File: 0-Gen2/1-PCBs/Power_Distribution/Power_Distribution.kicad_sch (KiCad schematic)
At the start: 33 parts, among them IC1 ACS713ELCTR-30A-T, IC2 ACS713ELCTR-30A-T, IC3 ACS713ELCTR-30A-T, IC4 ACS713ELCTR-30A-T, IC5 ACS713ELCTR-30A-T, IC6 ACS713ELCTR-30A-T, IC7 ACS713ELCTR-30A-T, IC8 ACS713ELCTR-30A-T, J1 1098169, J2 1098169, J3 Conn_01x08, J4 1986660-2, J5 Conn_01x06, J6 1098169, J7 1098169, J8 Conn_01x02, J9 Conn_01x08

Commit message: [add] MLU2 progress, [bugfix] depth sensor
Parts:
- removed J5: Conn_01x06, Connector_PinHeader_2.54mm:PinHeader_1x06_P2.54mm_Vertical, symbol Connector_Generic:Conn_01x06
- removed J8: Conn_01x02, Connector_PinHeader_2.54mm:PinHeader_1x02_P2.54mm_Vertical, symbol Connector_Generic:Conn_01x02
- added Cf10, Cf11, Cf12, Cf13, Cf14, Cf15, Cf16, Cf9: 100 µF, Capacitor_SMD:C_0805_2012Metric_Pad1.18x1.45mm_HandSolder, symbol Device:C
- added H1: IDC Cable, symbol Mechanical:MountingHole
- added J10, J11, J12, J13, J14, J15, J16, J17: 430450228, Imported_Footprints:CONN_SD-43045-010_02_MOL, symbol Imported:430450228
- added J18: SBH11-PBPC-D10-ST-BK, Imported_Footprints:SULLINS_SBH11-PBPC-D10-ST-BK, symbol Imported_Symbols:SBH11-PBPC-D10-ST-BK
- added JP1, JP2: Jumper_2_Bridged, Jumper:SolderJumper-2_P1.3mm_Bridged2Bar_RoundedPad1.0x1.5mm, symbol Jumper:Jumper_2_Bridged
- added LED1, LED10, LED11, LED12, LED2, LED3, LED4, LED5, LED6, LED7, LED8, LED9: 1655, LED_SMD:LED_LiteOn_LTST-E563C_PLCC4_5.0x5.0mm_P3.2mm_HandSoldering, symbol Imported_Symbols:1655
- added R1, R2: 10k, Resistor_SMD:R_0805_2012Metric_Pad1.20x1.40mm_HandSolder, symbol Device:R_US
- added U1, U2: MCP9808_MSOP, Package_SO:MSOP-8_3x3mm_P0.65mm, symbol Sensor_Temperature:MCP9808_MSOP
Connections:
- net COM: now also JP2.1 (A)
- net GND: now also Cf10.2, Cf11.2, Cf12.2, Cf13.2, Cf14.2, Cf15.2, Cf16.2, Cf9.2, J10.2, J11.2, J12.2, J13.2, J14.2, J15.2, J16.2, J17.2, J18.12, J18.20, JP2.2 (B), LED1.1 (VSS), LED10.1 (VSS), LED11.1 (VSS), LED12.1 (VSS), LED2.1 (VSS), LED3.1 (VSS), LED4.1 (VSS), LED5.1 (VSS), LED6.1 (VSS), LED7.1 (VSS), LED8.1 (VSS), LED9.1 (VSS), R1.2, R2.2, U1.4 (GND), U1.5 (A2), U2.4 (GND), U2.6 (A1)
- net REF: now also JP1.1 (A)
- net SCL: now also J18.2, U1.2 (SCL), U2.2 (SCL)
- net SDA: now also J18.4, U1.1 (SDA), U2.1 (SDA)
- net VIout1: now also Cf9.1
- net VIout2: now also Cf10.1
- net VIout3: now also Cf11.1
- net VIout4: now also Cf12.1
- net VIout5: now also Cf13.1
- net VIout6: now also Cf14.1
- net VIout7: now also Cf15.1
- net VIout8: now also Cf16.1
- net 5V renamed +5V
- net +5V: now also J18.14, J18.16, JP1.2 (B), LED1.3 (VDD), LED10.3 (VDD), LED11.3 (VDD), LED12.3 (VDD), LED2.3 (VDD), LED3.3 (VDD), LED4.3 (VDD), LED5.3 (VDD), LED6.3 (VDD), LED7.3 (VDD), LED8.3 (VDD), LED9.3 (VDD)
- new net: LED3.4 (DOUT), LED4.2 (DIN)
- new net: LED10.2 (DIN), LED9.4 (DOUT)
- new net: LED5.4 (DOUT), LED6.2 (DIN)
- new net: LED6.4 (DOUT), LED7.2 (DIN)
- new net: LED10.4 (DOUT), LED11.2 (DIN)
- new net: LED11.4 (DOUT), LED12.2 (DIN)
- new net: LED7.4 (DOUT), LED8.2 (DIN)
- new net: LED1.4 (DOUT), LED2.2 (DIN)
- new net +3.3V: J18.18, R1.1, R2.1, U1.6 (A1), U1.7 (A0), U1.8 (V_{DD}), U2.5 (A2), U2.7 (A0), U2.8 (V_{DD})
- new net NEO_PASS1: LED4.4 (DOUT), LED5.2 (DIN)
- new net NEO_PASS2: LED8.4 (DOUT), LED9.2 (DIN)
- new net PWM0: J10.1, J18.1
- new net PWM1: J12.1, J18.3
- new net PWM2: J14.1, J18.5
- new net PWM3: J16.1, J18.7
- new net PWM4: J11.1, J18.9
- new net PWM5: J13.1, J18.11
- new net PWM6: J15.1, J18.13
- new net PWM7: J17.1, J18.15
- new net outNEO_CTRL_MOOD: J18.8, LED12.4 (DOUT)
- new net outNEO_CTRL_SIG: J18.19, LED2.4 (DOUT)
- new net toNEO_CTRL_MOOD: J18.6, LED3.2 (DIN)
- new net toNEO_CTRL_SIG: J18.17, LED1.2 (DIN)
- no-connect marks 0 -> 5
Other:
- note added: "Analog noise filter"
- note added: "I2C @ 0x1B format: 0011(A2)(A1)(A0)"
- note added: "I2C @ 0x1D format: 0011(A2)(A1)(A0)"
- note added: "I2C @ 0x48"
- note added: "Integrated MCP9808 #1"
- note added: "Integrated MCP9808 #2"
- note added: "Interconnect to MLU"
- note added: "Leak sensor on this board? Humidity sensor on this board?"
- note added: "PWM Thruster Interface"
- note added: "Power Connectors To ESCs"
- note added: "https://learn.adafruit.com/adafruit-ads7830-8-channel-8-bit-adc/pinouts"
- note removed: "Connectors To ESCs"
- moved on the sheet: Cb1, Cb2, Cb3, Cb4, Cb5, Cb6, Cb7, Cb8, Cf1, Cf2, Cf3, Cf4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

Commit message: management2 updates
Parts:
- added JP3: Jumper_3_Bridged12, Jumper:SolderJumper-3_P1.3mm_Bridged2Bar12_RoundedPad1.0x1.5mm, symbol Jumper:Jumper_3_Bridged12
- added R3: 2.2k Array, Imported_Footprints:RES_EXB2HV_1506x8, symbol Imported_Symbols:EXB-2HV222JV
- added R4: 3.9k Array, Imported_Footprints:RES_EXB2HV_1506x8, symbol Imported_Symbols:EXB-2HV222JV
- Cf1: value 100 µF -> 100 nF; Supplier 1 https://www.digikey.com/en/products/detail/murata-electroni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 -> https://www.digikey.com/en/products/detail/yageo/CC0805KRX7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; Supplier 1 S/N 490-13980-1-ND -> 311-1140-1-ND
- Cf10, Cf11, Cf12, Cf13, Cf14, Cf15, Cf16, Cf9: value 100 µF -> 1 µF; Supplier 1 https://www.digikey.com/en/products/detail/murata-electroni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 -> https://www.digikey.com/en/products/detail/samsung-electro-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; Supplier 1 S/N 490-13980-1-ND -> 1276-1029-1-ND
- Cf2, Cf3, Cf4, Cf5, Cf6, Cf7, Cf8: value 100 µF -> 100nF; Supplier 1 https://www.digikey.com/en/products/detail/murata-electroni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 -> https://www.digikey.com/en/products/detail/yageo/CC0805KRX7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; Supplier 1 S/N 490-13980-1-ND -> 311-1140-1-ND
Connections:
- net +3.3V: now also JP1.2 (B), JP3.2 (C)
- net +5V: now also JP3.3 (B); no longer J3.1 (Pin_1), JP1.2 (B)
- net GND: now also R4.10, R4.11, R4.12, R4.13, R4.14, R4.15, R4.16, R4.9
- net VIout1: now also R3.1; no longer J9.8 (Pin_8)
- net VIout2: now also R3.2; no longer J9.7 (Pin_7)
- net VIout3: now also R3.3; no longer J9.6 (Pin_6)
- net VIout4: now also R3.4; no longer J9.5 (Pin_5)
- net VIout5: now also R3.5; no longer J9.4 (Pin_4)
- net VIout6: now also R3.6; no longer J9.3 (Pin_3)
- net VIout7: now also R3.7; no longer J9.2 (Pin_2)
- net VIout8: now also R3.8; no longer J9.1 (Pin_1)
- new net: J3.1 (Pin_1), JP3.1 (A)
- new net VIout1Div: J9.8 (Pin_8), R3.16, R4.1
- new net VIout2Div: J9.7 (Pin_7), R3.15, R4.2
- new net VIout3Div: J9.6 (Pin_6), R3.14, R4.3
- new net VIout4Div: J9.5 (Pin_5), R3.13, R4.4
- new net VIout5Div: J9.4 (Pin_4), R3.12, R4.5
- new net VIout6Div: J9.3 (Pin_3), R3.11, R4.6
- new net VIout7Div: J9.2 (Pin_2), R3.10, R4.7
- new net VIout8Div: J9.1 (Pin_1), R3.9, R4.8
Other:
- note added: "0x1B --> Temp Left 0x1D --> Temp Right 0x48 --> x8 ADC"
- note added: "3.3V reference -> 12.9mV resolution -> 149mA resolution/thruster"
- note added: "5V or 3.3V, sets I2C output and Vanalog range"
- note added: "Convert 5V analog output logic to 3.3V Min resistance is 4.9k. Spec to 6.2k Rdiv = 0.645 (5V --> 3.225V)"
- note removed: "Leak sensor on this board? Humidity sensor on this board?"
- moved on the sheet: Cb1, Cb2, Cb3, Cb4, Cb5, Cb6, Cb7, Cb8, Cf1, Cf2, Cf3, Cf4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

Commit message: almost done with all orders
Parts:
- removed J4: 1986660-2, Imported_Footprints:TE_1986660-2, symbol HighPowerRoboConnector:1986660-2
- added J4: Conn_01x02_Pin, Connector_AMASS:AMASS_XT60IPW-M_1x03_P7.20mm_Horizontal, symbol Connector:Conn_01x02_Pin
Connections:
- net +BATT: now also J4.2 (Pin_2)
- net -BATT: now also J4.1 (Pin_1)
- net toNEO_CTRL_MOOD: now also LED1.2 (DIN); no longer LED3.2 (DIN)
- net outNEO_CTRL_SIG: no longer names the net of J18.19
- net outNEO_CTRL_SIG: no longer LED2.4 (DOUT)
- net toNEO_CTRL_SIG: no longer names the net of J18.17
- net toNEO_CTRL_SIG: no longer LED1.2 (DIN)
- new net: LED2.4 (DOUT), LED3.2 (DIN)
- no-connect marks 5 -> 7

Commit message: ready for fab
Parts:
- added H2, H3, H4: MountingHole, MountingHole:MountingHole_3.2mm_M3, symbol Mechanical:MountingHole
- R3: footprint Imported_Footprints:RES_EXB2HV_1506x8 -> Imported_Footprints:2506_8x_Resistor_Array; Supplier 1 https://www.digikey.com/en/products/detail/panasonic-electr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 -> https://www.digikey.com/en/products/detail/cts-resistor-pro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; Supplier 1 S/N Y1222CT-ND -> 60-742C163222JPCT-ND
- R4: value 3.9k Array -> 3.3k Array; footprint Imported_Footprints:RES_EXB2HV_1506x8 -> Imported_Footprints:2506_8x_Resistor_Array; Supplier 1 https://www.digikey.com/en/products/detail/panasonic-electr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 -> https://www.digikey.com/en/products/detail/cts-resistor-pro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; Supplier 1 S/N Y1392CT-ND -> 60-742C163332JPCT-ND
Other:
- note added: "Convert 5V analog output logic to 3.3V Min resistance is 4.9k. Spec to 5.5k Rdiv = 0.6 (5V --> 3V)"
- note removed: "Convert 5V analog output logic to 3.3V Min resistance is 4.9k. Spec to 6.2k Rdiv = 0.645 (5V --> 3.225V)"

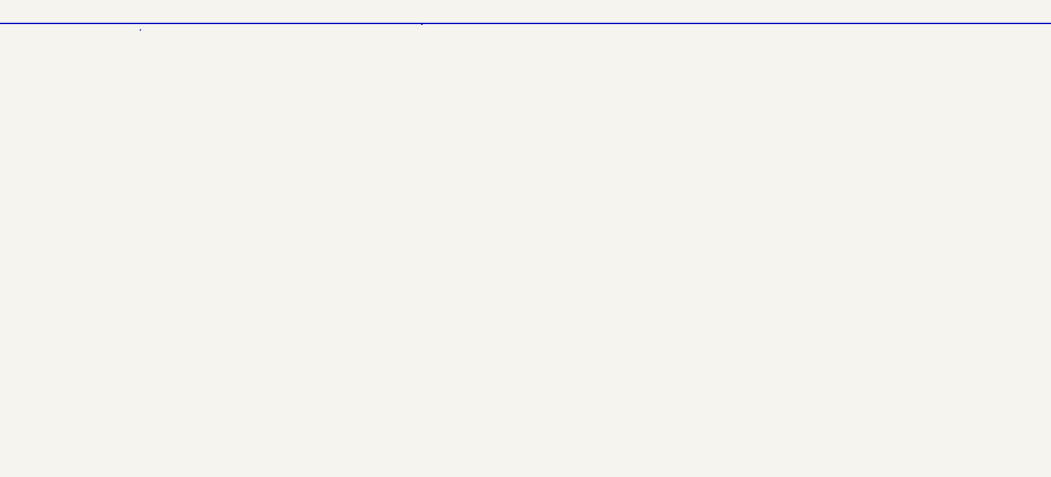
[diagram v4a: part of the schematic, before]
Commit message: [bugfixing] board bringup
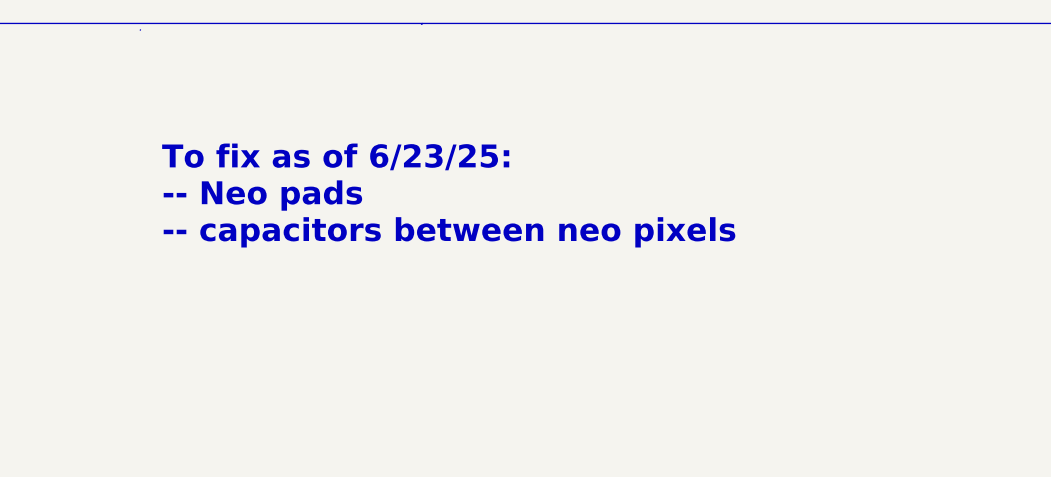
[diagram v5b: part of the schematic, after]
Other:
- note added: "To fix as of 6/23/25: -- Neo pads -- capacitors between neo pixels"
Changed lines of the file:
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@@
+		)
+	)
+	(text "To fix as of 6/23/25:\n-- Neo pads\n-- capacitors between neo pixels"
+		(exclude_from_sim no)
+		(at 236.347 31.623 0)
+		(effects
+			(font
+				(size 2.54 2.54)
+				(thickness 0.508)
+				(bold yes)
+				(color 132 0 0 1)
+			)
+			(justify left)
 		)
 	)
